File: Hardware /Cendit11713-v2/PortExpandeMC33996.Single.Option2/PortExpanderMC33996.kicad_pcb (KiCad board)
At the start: 2 copper layers, 13 parts, among them J1 DEBUG_CONN, P1 VIKING_HEADER_9P, P2 VIKING_HEADER_9P, U1 MC33996EKR2

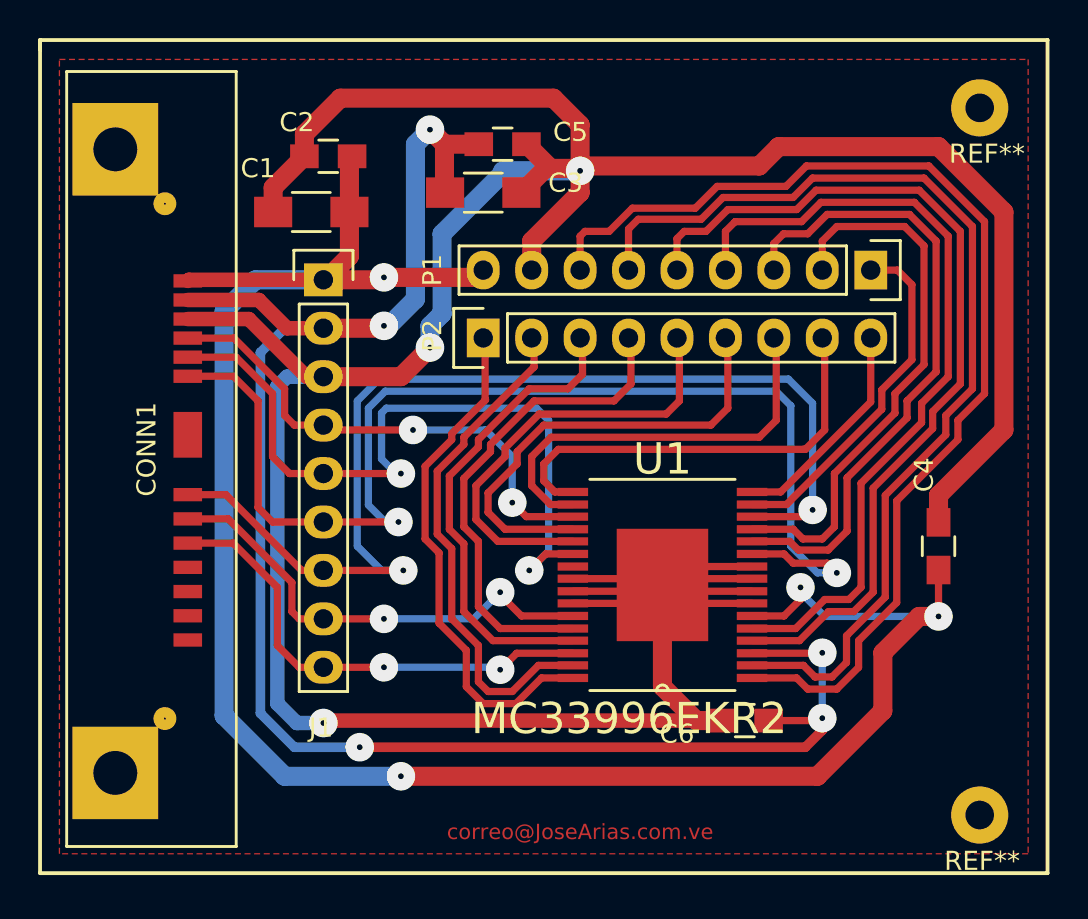
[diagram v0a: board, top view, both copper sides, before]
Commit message: En CenditLab + Cendit11713
  - Edicion de PCB tarjeta madre
  - Revision de PCB expansor Viking
  - Archivos gerber generados

  - Edicion de clases UI
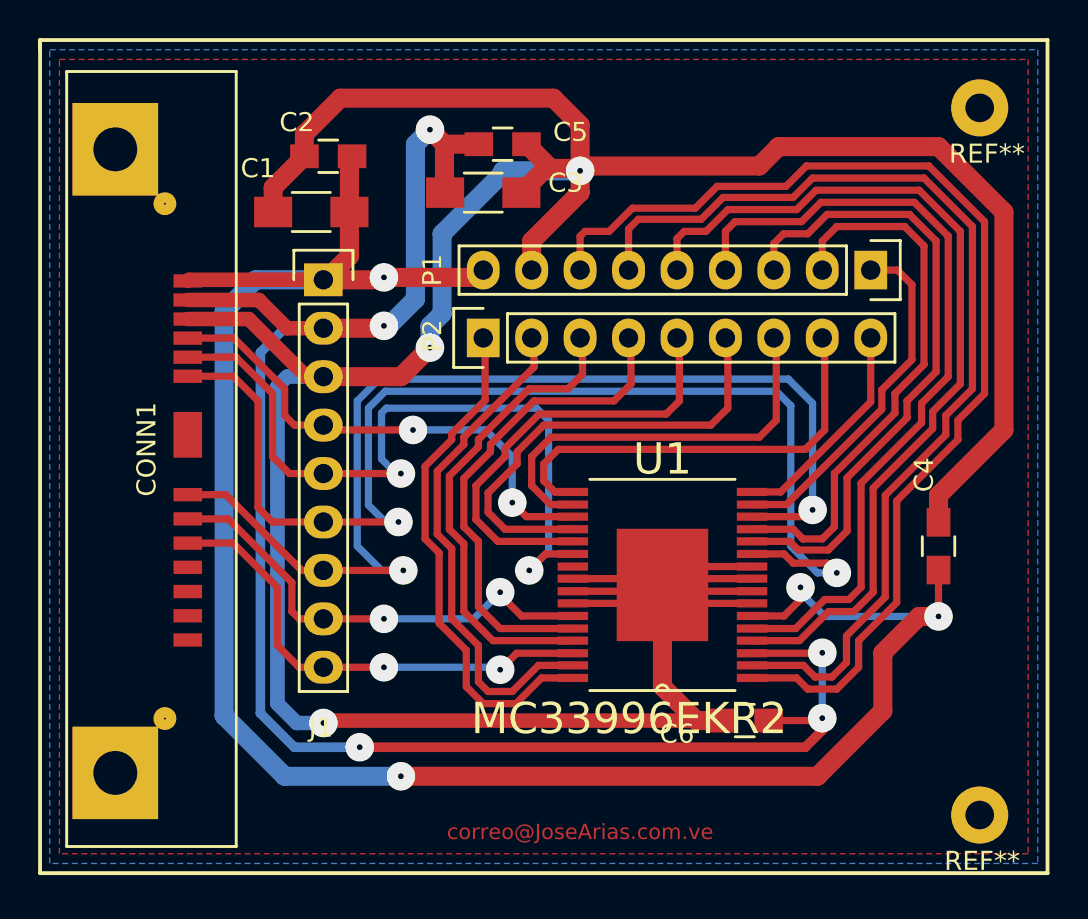
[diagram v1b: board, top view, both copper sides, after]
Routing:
- added copper zone on B.Cu, net GNDPWR
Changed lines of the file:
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@@
-(kicad_pcb (version 4) (host pcbnew 4.0.5+dfsg1-4~bpo8+1)
+(kicad_pcb (version 4) (host pcbnew 4.0.6-e0-6349~53~ubuntu14.04.1)
   (general
     (links 55)
@@
   )
   (setup
-    (last_trace_width 1)
+    (last_trace_width 0.25)
     (user_trace_width 0.35)
     (user_trace_width 0.381)
@@
     (user_trace_width 5)
     (trace_clearance 0.2)
-    (zone_clearance 1)
+    (zone_clearance 0.6)
     (zone_45_only yes)
     (trace_min 0.2)
@@
       )
     )
+  )
+  (zone (net 1) (net_name GNDPWR) (layer B.Cu) (hatch edge 0.508)
+    (connect_pads (clearance 0.6))
+    (min_thickness 0.3)
+    (fill yes (arc_segments 16) (thermal_gap 1) (thermal_bridge_width 0.6))
+    (polygon
+      (pts
+        (xy 143.764 121.412) (xy 91.948 121.412) (xy 91.948 78.74) (xy 143.764 78.74)
+      )
+    )

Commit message: Trabajo en CenditLab + Cendit11713
  - Diseño + codigo UI
  - PCBs tarjeta madre + puertos Viking
  - Se generan Gerber para solicitud de prototipos PCB
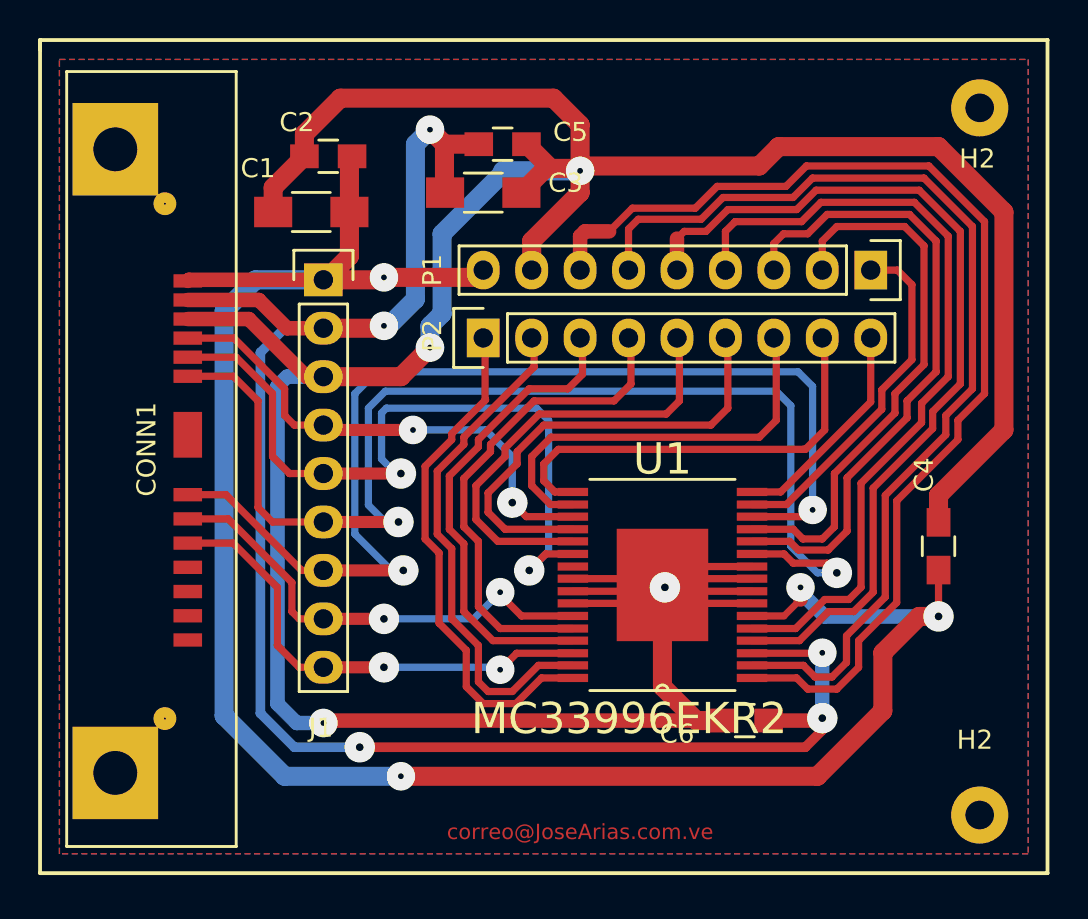
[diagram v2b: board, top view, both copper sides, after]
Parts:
- renumbered REF** to H2
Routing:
- net //CS: track 57.3 -> 58.2 mm
- net GNDPWR: track 192.9 -> 193.0 mm, vias 3 -> 4
